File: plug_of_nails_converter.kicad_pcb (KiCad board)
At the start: 2 copper layers, 44.8 x 31.7 mm, 6 parts, among them J1 5103308-1, J2 B-2100S10P-B110

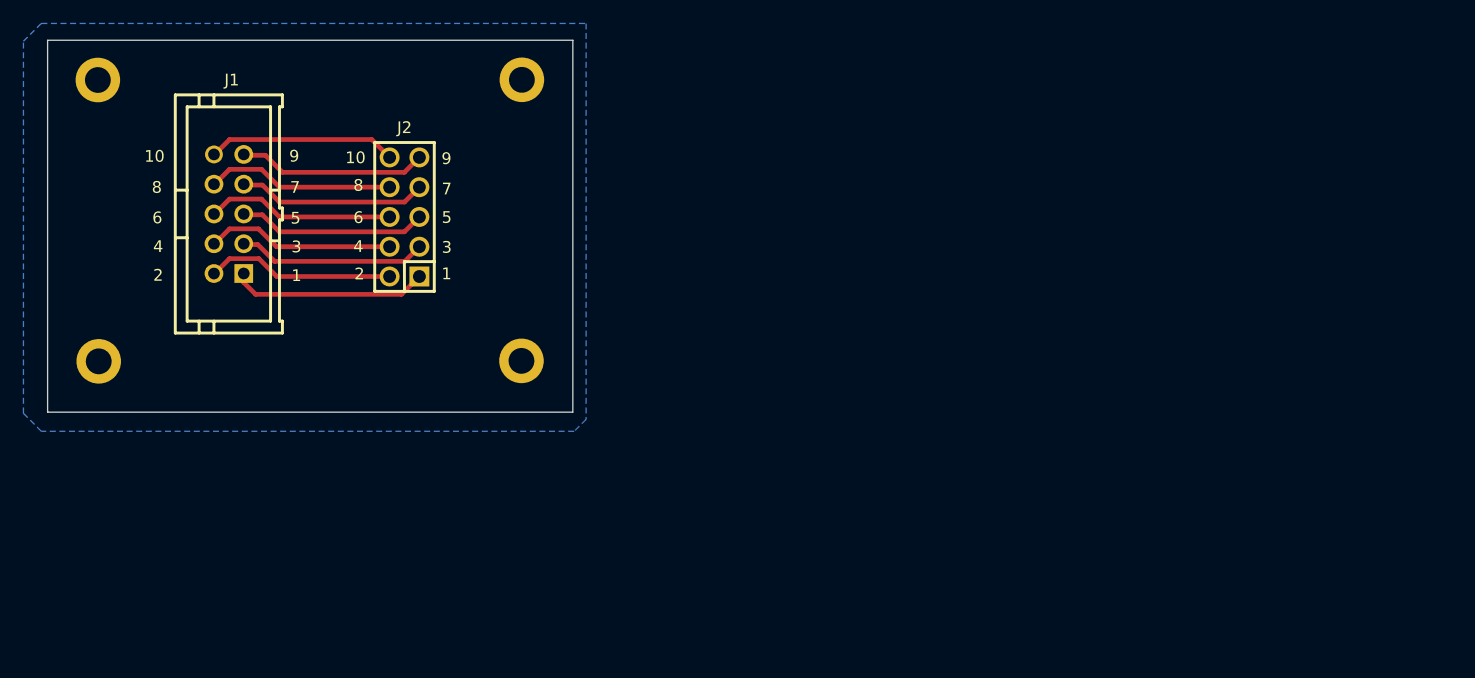
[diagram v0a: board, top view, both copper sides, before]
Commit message: Component library added as submodule
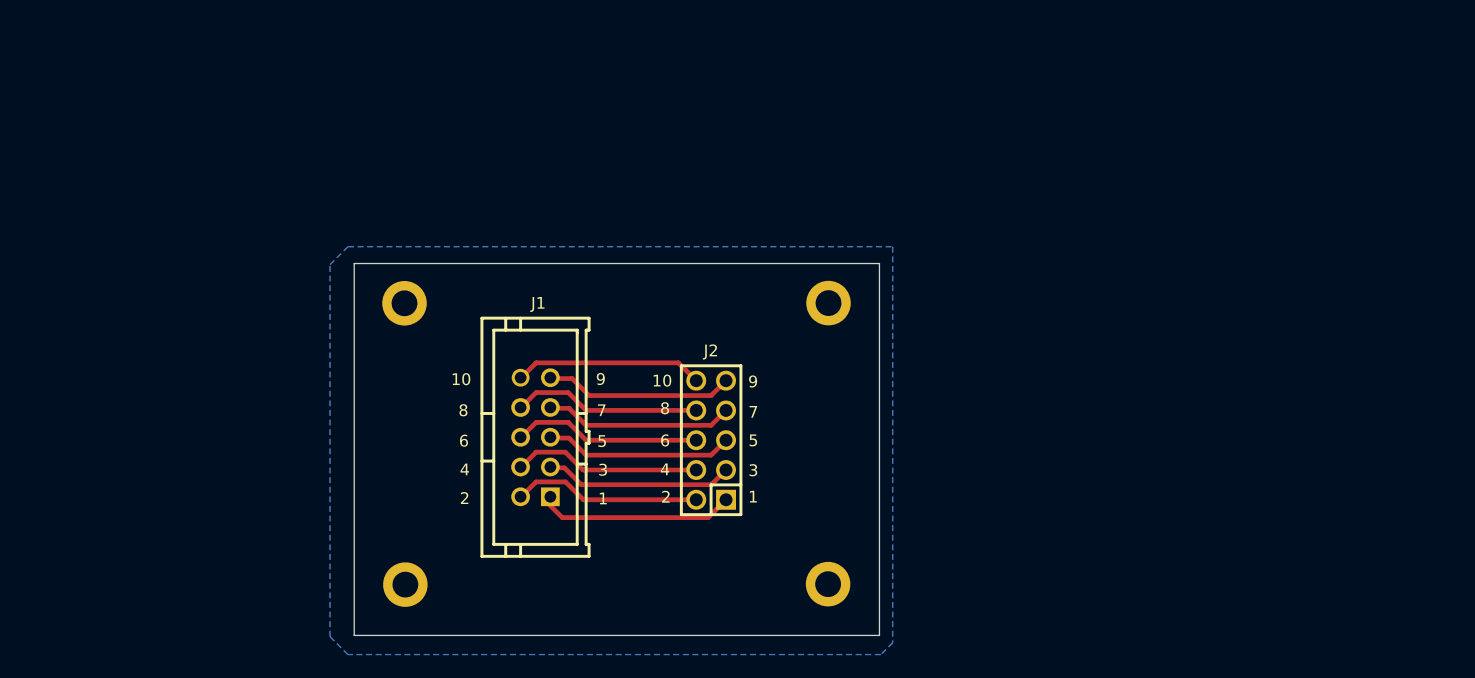
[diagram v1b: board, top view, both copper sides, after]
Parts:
- moved J2 32.4 mm to (164.3, 87.4)
- moved MH4 32.4 mm to (138.2, 99.7)
- moved MH2 32.4 mm to (174.4, 75.7)
- moved J1 32.4 mm to (149.4, 87.1)
- moved MH3 32.4 mm to (174.3, 99.7)
- moved MH1 32.4 mm to (138.2, 75.7)
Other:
- board text added: "0"
- board text added: "0 mm"
- board text added: "0.0000 mm / 0.0000 mm"
- board text added: "0.01 mm"
- board text added: "0.02"
- board text added: "0.035 mm"
- board text added: "0.3000 mm"
- board text added: "1.51 mm"
- board text added: "1.6000 mm"
- board text added: "3.3"
- board text added: "4.5"
- board text added: "44.8125 mm x 31.7312 mm"
- board text added: "B.Cu"
- board text added: "B.Mask"
- board text added: "B.Paste"
- board text added: "B.Silkscreen"
- board text added: "BOARD CHARACTERISTICS"
- board text added: "Board Thickness:"
- board text added: "Board overall dimensions:"
- board text added: "Bottom Silk Screen"
- board text added: "Bottom Solder Mask"
- board text added: "Bottom Solder Paste"
- board text added: "Castellated pads:"
- board text added: "Color"
- board text added: "Copper Finish:"
- board text added: "Copper Layer Count:"
- board text added: "Dielectric"
- board text added: "Edge card connectors:"
- board text added: "Epsilon R"
- board text added: "F.Cu"
- board text added: "F.Mask"
- board text added: "F.Paste"
- board text added: "F.Silkscreen"
- board text added: "FR4"
- board text added: "Impedance Control:"
- board text added: "Layer Name"
- board text added: "Loss Tangent"
- board text added: "Material"
- board text added: "Min hole diameter:"
- board text added: "Min track/spacing:"
- board text added: "No"
- board text added: "None"
- board text added: "Not specified"
- board text added: "Plated Board Edge:"
- board text added: "Thickness (mm)"
- board text added: "Top Silk Screen"
- board text added: "Top Solder Mask"
- board text added: "Top Solder Paste"
- board text added: "Type"
- board text added: "copper"
- board text added: "core"

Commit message: Version v3.0 with JLink Edu support
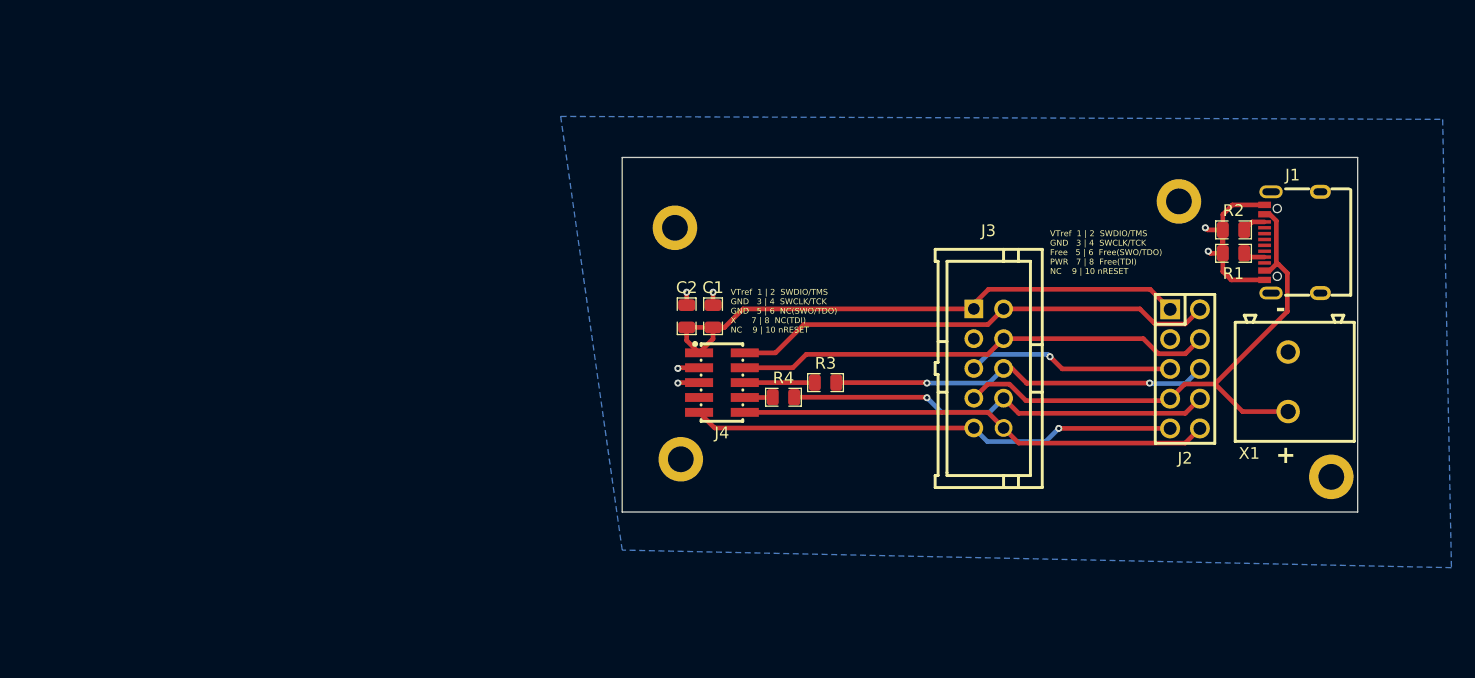
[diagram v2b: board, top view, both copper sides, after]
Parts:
- added C1: CC0805KRX7R9BB104, pepy_sym_lib:[CAP_SMD_0805_2012Metric], F.Cu at (164.5, 76.8)
- added C2: CL21A106KOQNNNE, pepy_sym_lib:[CAP_SMD_0805_2012Metric], F.Cu at (162.2, 76.8)
- added J3: 5103308-1, pepy_sym_lib:[10P_2X5_IDC_MALE]TE Connectivity 5103308-1, F.Cu at (188.0, 81.2)
- added J4: 20021121-00010T4LF, pepy_sym_lib:[10P_2X5_IDC_1_27MM_MALE]Amphenol ICC 20021121-00010T4LF, F.Cu at (165.3, 82.5)
- added R1: 0805W8F5101T5E, pepy_sym_lib:[RES_SMD_0805_2012Metric], F.Cu at (208.9, 71.4)
- added R2: 0805W8F5101T5E, pepy_sym_lib:[RES_SMD_0805_2012Metric], F.Cu at (208.9, 69.4)
- added R3: 0805W8F0000T5E, pepy_sym_lib:[RES_SMD_0805_2012Metric], F.Cu at (174.1, 82.5)
- added R4: 0805W8F0000T5E, pepy_sym_lib:[RES_SMD_0805_2012Metric], F.Cu at (170.5, 83.7)
- added X1: WJ500V-5.08-2P-14-00A, pepy_sym_lib:[1x2_SCREW_TERMINAL_BLOCK]Ningbo Kangnex Elec WJ500V-5.08-2P, F.Cu at (213.6, 82.4)
- J1: value 5103308-1 -> TYPE-C 16PIN 2MD(073); footprint pepy_sym_lib:[10P_2X5_IDC_MALE]TE Connectivity 5103308-1 -> pepy_sym_lib:[USB_C_16P_RA_FEMALE]SHOU HAN TYPE-C 16PIN 2MD(073)
- moved J1 66.7 mm to (213.9, 70.5), turned to 90 degrees
- moved MH3 43.9 mm to (217.2, 90.5)
- moved J2 40.9 mm to (204.8, 81.3), turned to -90 degrees
- moved MH2 31.1 mm to (204.2, 67.0)
- moved MH4 25.8 mm to (161.8, 89.0)
- moved MH1 24.0 mm to (161.2, 69.2)
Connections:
- J1 pad 1: /P1 -> GND
- J1 pad 10: /P10 -> Net-(J1-CC2)
- J1 pad 2: /P2 -> PWR
- J1 pad 3: /P3 -> unconnected-(J1-SBU2-Pad3)
- J1 pad 4: /P4 -> Net-(J1-CC1)
- J1 pad 5: /P5 -> unconnected-(J1-DN2-Pad5)
- J1 pad 6: /P6 -> unconnected-(J1-DP1-Pad6)
- J1 pad 7: /P7 -> unconnected-(J1-DN1-Pad7)
- J1 pad 8: /P8 -> unconnected-(J1-DP2-Pad8)
- J1 pad 9: /P9 -> unconnected-(J1-SBU1-Pad9)
- J2 pad 3: /P3 -> GND
- J2 pad 7: /P7 -> PWR
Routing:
- net PWR: track 0.00 -> 48.9 mm
- net /P1: track 16.7 -> 48.8 mm
- net /P9: track 16.1 -> 41.7 mm, vias 0 -> 1
- net /P2: track 16.2 -> 41.4 mm
- net /P4: track 16.2 -> 40.9 mm
- net /P10: track 16.2 -> 40.4 mm
- net GND: track 0.00 -> 23.4 mm, vias 0 -> 6
- net /P8: track 16.2 -> 36.7 mm, vias 0 -> 1
- net /P6: track 16.2 -> 32.7 mm, vias 0 -> 2
- net /P7: track 16.1 -> 0.00 mm
- net /P3: track 16.1 -> 0.00 mm
- net Net-(J4-Pad6): track 0.00 -> 5.97 mm
- net Net-(J4-Pad8): track 0.00 -> 2.40 mm
- net Net-(J1-CC2): track 0.00 -> 2.02 mm
- net Net-(J1-CC1): track 0.00 -> 1.87 mm
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- added copper zone on B.Cu, net GND
- removed copper zone on B.Cu, net (none)
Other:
- board size 44.8 x 31.7 mm -> 62.8 x 30.2 mm
- board text added: "+"
- board text added: "-"
- board text added: "Plug of nails converter v3, perseluspy"
- board text added: "VTref 1 | 2 SWDIO/TMS GND 3 | 4 SWCLK/TCK Free 5 | 6 Free(SWO/TDO) PWR 7 | 8 Free(TDI) NC 9 | 10 nRESET"
- board text added: "VTref 1 | 2 SWDIO/TMS GND 3 | 4 SWCLK/TCK GND 5 | 6 NC(SWO/TDO) X 7 | 8 NC(TDI) NC 9 | 10 nRESET"
- board text removed: "10"
- board text removed: "3"
- board text removed: "4"
- board text removed: "5"
- board text removed: "6"
- board text removed: "7"
- board text removed: "8"
- board text removed: "9"
- board text removed: "Plug of nails converter v2, perseluspy"
